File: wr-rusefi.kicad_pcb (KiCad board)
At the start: 2 copper layers, 88.9 x 78.7 mm, 114 parts, among them P101 USB_OTG, P102 CONN_02X20, Q401 IRF540N, Q402 IRF540N, Q403 IRF540N, Q404 IRF540N, Q405 IRF540N, Q406 IRF540N, U101 ISL89410, U102 ISL89410, U103 FT230XS, U104 STM32F373CCTx, U105 MCP2562-E/SN, U106 LD1117S33TR, U107 MAX9924, U201 LM324, U301 LM324, U501 LM2576xx

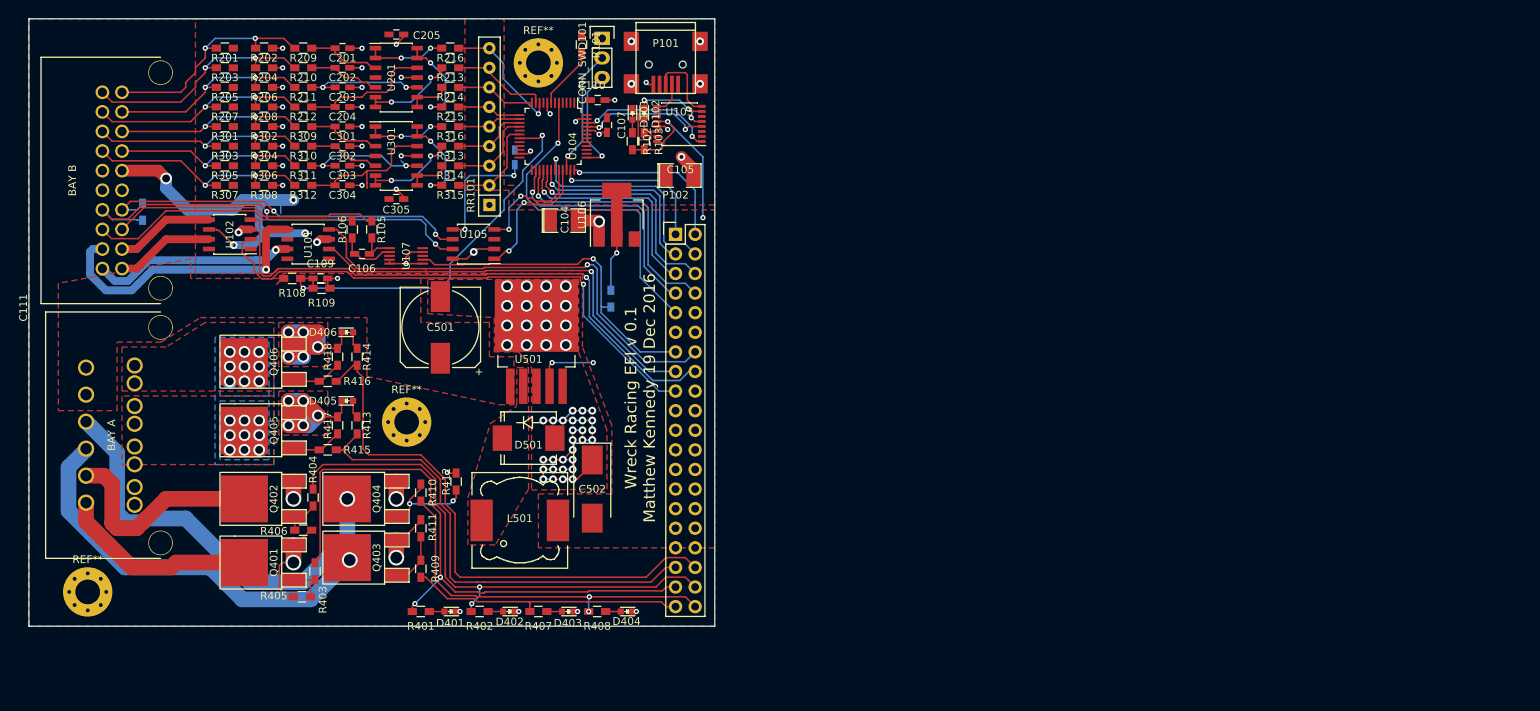
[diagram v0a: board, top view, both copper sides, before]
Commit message: Rework most of board for rusefi
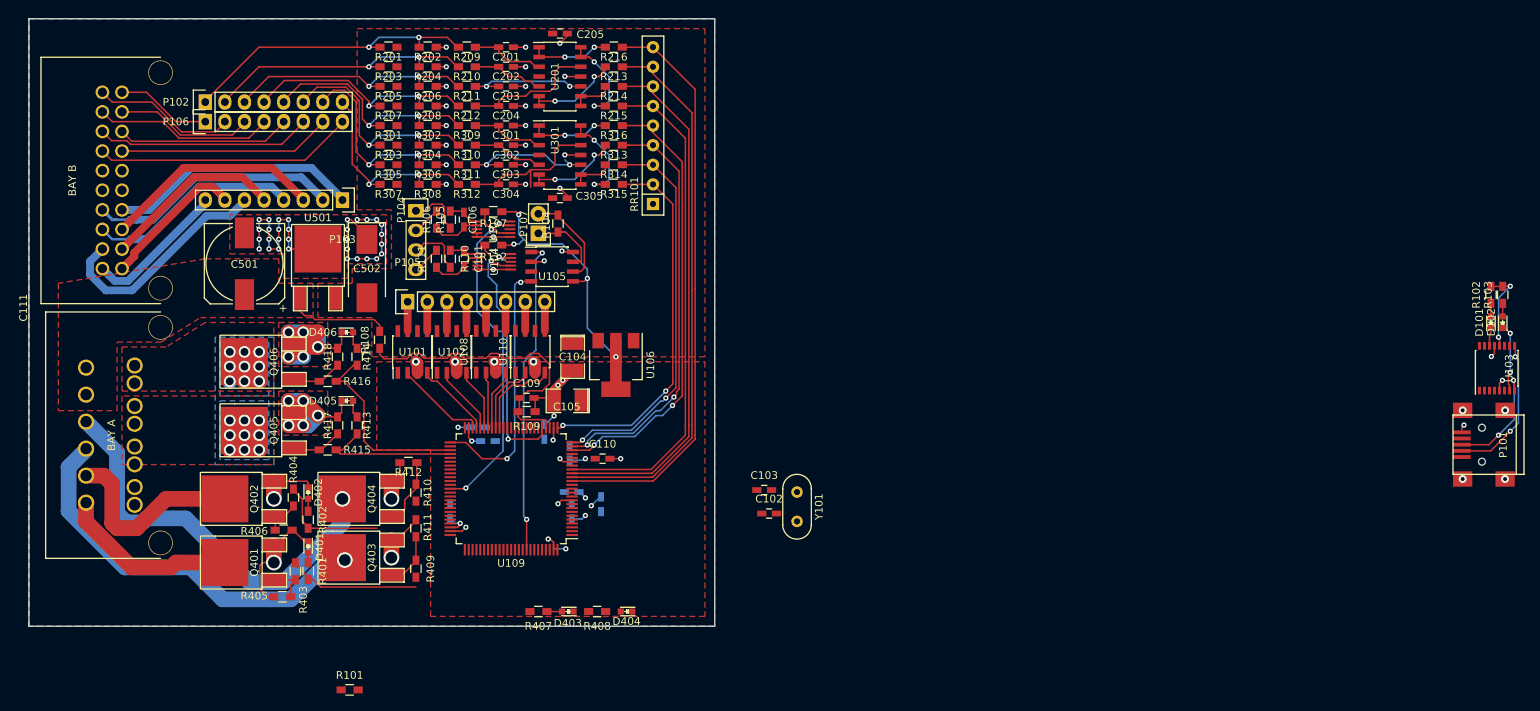
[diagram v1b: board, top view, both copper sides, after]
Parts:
- removed CONN_SWD101: CONN_01X03, Pin_Headers:Pin_Header_Straight_1x03
- removed D501: D_Schottky, Diodes_SMD:SMC_Standard
- removed L501: 38uH, Choke_SMD:Choke_SMD_12x12mm_h6mm
- removed REF** (x3): MountingHole_3.2mm_M3_Pad_Via, Mounting_Holes:MountingHole_3.2mm_M3_Pad_Via
- removed REF***: KiCad-Logo2_12mm_SilkScreen, Symbols:KiCad-Logo2_12mm_SilkScreen
- removed REF***: OSHW-Logo_11.4x12mm_SilkScreen, Symbols:OSHW-Logo_11.4x12mm_SilkScreen
- added C101: 1nF, Capacitors_SMD:C_0603_HandSoldering, F.Cu at (125.0, 83.8)
- added C102: 20pF, Capacitors_SMD:C_0603_HandSoldering, F.Cu at (164.5, 116.8)
- added C103: 20pF, Capacitors_SMD:C_0603_HandSoldering, F.Cu at (163.9, 113.8)
- added C112: 2.2uF, Capacitors_SMD:C_0603_HandSoldering, B.Cu at (128.1, 107.4)
- added C113: 2.2uF, Capacitors_SMD:C_0603_HandSoldering, B.Cu at (123.2, 116.5)
- added C114: .1uF, Capacitors_SMD:C_0603_HandSoldering, B.Cu at (135.4, 106.2)
- added C115: .1uF, Capacitors_SMD:C_0603_HandSoldering, B.Cu at (138.9, 114.0)
- added C116: .1uF, Capacitors_SMD:C_0603_HandSoldering, B.Cu at (138.9, 116.6)
- added C117: 4.7uF, Capacitors_SMD:C_0603_HandSoldering, B.Cu at (142.7, 115.6)
- added P103: CONN_01X08, Socket_Strips:Socket_Strip_Straight_1x08, F.Cu at (109.2, 76.2)
- added P104: CONN_01X04, Socket_Strips:Socket_Strip_Straight_1x04, F.Cu at (118.7, 77.6)
- added P105: CONN_01X08, Socket_Strips:Socket_Strip_Straight_1x08, F.Cu at (117.7, 89.4)
- added P106: CONN_01X08, Socket_Strips:Socket_Strip_Straight_1x08, F.Cu at (91.4, 66.0)
- added P107: CONN_01X02, Socket_Strips:Socket_Strip_Straight_1x02, F.Cu at (134.6, 80.5)
- added R110: 10k, Resistors_SMD:R_0603_HandSoldering, F.Cu at (123.2, 83.8)
- added R111: 10k, Resistors_SMD:R_0603_HandSoldering, F.Cu at (121.4, 83.8)
- added R112: 10k, Resistors_SMD:R_0603_HandSoldering, F.Cu at (128.8, 82.0)
- added U108: ISL89410, Housings_SOIC:SOIC-8_3.9x4.9mm_Pitch1.27mm, F.Cu at (128.5, 95.9)
- added U109: STM32F407VGTx, Housings_QFP:LQFP-100_14x14mm_Pitch0.5mm, F.Cu at (131.1, 113.6)
- added U110: ISL89410, Housings_SOIC:SOIC-8_3.9x4.9mm_Pitch1.27mm, F.Cu at (133.6, 95.9)
- added Y101: Crystal, Crystals:Crystal_HC52-6mm_Vertical, F.Cu at (168.1, 114.1)
- C107: moved to B.Cu
- P102: value CONN_02X20 -> CONN_01X08; footprint Pin_Headers:Pin_Header_Straight_2x20 -> Socket_Strips:Socket_Strip_Straight_1x08
- R104, R107: moved to F.Cu
- U104: value STM32F373CCTx -> MAX9924; footprint Housings_QFP:LQFP-48_7x7mm_Pitch0.5mm -> wr-efi:uMAX-10
- U501: value LM2576xx -> LM7805CT; footprint TO_SOT_Packages_SMD:TO-263-5Lead -> TO_SOT_Packages_SMD:TO-252-2Lead
- moved P101 117.8 mm to (257.8, 107.9), turned to 180 degrees
- moved D101 114.5 mm to (258.1, 92.0), turned to 90 degrees
- moved D102 114.5 mm to (259.6, 92.0), turned to 90 degrees
- moved R102 113.1 mm to (258.1, 88.5), turned to 90 degrees
- moved R103 113.1 mm to (259.6, 88.5), turned to 90 degrees
- moved U103 110.6 mm to (258.9, 98.0), turned to 90 degrees
- moved R101 88.9 mm to (110.2, 139.7), turned to 0 degrees
- moved P102 63.3 mm to (91.4, 63.5)
- moved R104 53.9 mm to (137.2, 79.2)
- moved C110 46.5 mm to (142.9, 109.7)
- moved C107 42.6 mm to (126.8, 105.7), turned to 0 degrees
- moved C502 40.9 mm to (112.4, 85.1)
- moved C108 38.9 mm to (138.7, 109.0)
- moved C105 32.6 mm to (138.4, 102.2), turned to 180 degrees
- moved U102 32.6 mm to (123.4, 95.9), turned to 90 degrees
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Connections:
- C111 pad 11: IGN_A_OUT -> Net-(C111-Pad11)
- C111 pad 12: IGN_B_OUT -> Net-(C111-Pad12)
- C111 pad 13: VR- -> Net-(C111-Pad13)
- C111 pad 14: CANH -> Net-(C111-Pad14)
- C111 pad 17: AIN7 -> Net-(C111-Pad17)
- C111 pad 18: AIN5 -> Net-(C111-Pad18)
- C111 pad 19: AIN3 -> Net-(C111-Pad19)
- C111 pad 20: AIN1 -> Net-(C111-Pad20)
- C111 pad 21: IGN_C_OUT -> Net-(C111-Pad21)
- C111 pad 22: IGN_D_OUT -> Net-(C111-Pad22)
- C111 pad 23: VR+ -> Net-(C111-Pad23)
- C111 pad 24: CANL -> Net-(C111-Pad24)
- C111 pad 27: AIN6 -> Net-(C111-Pad27)
- C111 pad 28: AIN4 -> Net-(C111-Pad28)
- C111 pad 29: AIN2 -> Net-(C111-Pad29)
- C111 pad 30: AIN0 -> Net-(C111-Pad30)
- P102 pad 1: FPGA_G2 -> AIN0
- P102 pad 2: FPGA_G1 -> AIN1
- P102 pad 3: FPGA_G4 -> AIN2
- P102 pad 4: FPGA_G3 -> AIN3
- P102 pad 5: FPGA_SCK -> AIN4
- P102 pad 6: FPGA_G5 -> AIN5
- P102 pad 7: FPGA_MISO -> AIN6
- P102 pad 8: FPGA_MOSI -> AIN7
- R105 pad 2: VR+ -> VR1+
- R106 pad 2: VR- -> VR1-
- R107 pad 1: VRIN -> VRIN1
- U104 pad 1: +3V3 -> Net-(C101-Pad1)
- U104 pad 10: a0 -> +5V
- U104 pad 4: Net-(U104-Pad4) -> GND
- U104 pad 5: FPGA_MCU_CLK -> GND
- U104 pad 6: Net-(U104-Pad6) -> GND
- U104 pad 7: Net-(R101-Pad2) -> VRIN2
- U104 pad 8: GND -> Net-(U104-Pad8)
- U104 pad 9: +3V3 -> GND
- U107 pad 7: VRIN -> VRIN1
- U501 pad 2: Net-(D501-Pad1) -> GND
- U501 pad 3: GND -> +5V
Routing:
- net +5V: track 82.7 -> 10.9 mm, vias 8 -> 2
- net IGN_D_IN: track 74.3 -> 8.08 mm, vias 1 -> 0
- net IGN_C_IN: track 70.2 -> 8.93 mm, vias 1 -> 0
- net ls_1: track 77.9 -> 17.5 mm, vias 2 -> 0
- net a1: track 12.8 -> 71.8 mm
- net a0: track 16.6 -> 75.4 mm, vias 1 -> 0
- net a2: track 10.3 -> 68.4 mm
- net a3: track 8.32 -> 64.9 mm
- net ls_2: track 69.9 -> 14.8 mm, vias 2 -> 0
- net IGN_B_IN: track 60.3 -> 10.2 mm, vias 1 -> 0
- net a4: track 8.29 -> 57.8 mm, vias 0 -> 2
- net ls_4: track 48.0 -> 0.00 mm, vias 2 -> 0
- net INJ_B_IN: track 72.7 -> 25.2 mm
- net CANH: track 56.1 -> 9.31 mm, vias 2 -> 0
- net VRIN1: track 0.00 -> 45.5 mm, vias 0 -> 2
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- removed copper zone on F.Cu, net Net-(D501-Pad1)
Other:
- board text removed: "Wreck Racing EFI v 0.1 Matthew Kennedy 19 Dec 2016"

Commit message: Board mostly complete
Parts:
- added P108: USB_OTG, Connect:USB_Mini-B, F.Cu at (152.1, 124.3)
- added P109: CONN_01X02, Socket_Strips:Socket_Strip_Straight_1x02, F.Cu at (126.0, 126.7)
- added P110: CONN_01X06, Socket_Strips:Socket_Strip_Straight_1x06, F.Cu at (119.6, 129.3)
- added R113: 10k, Resistors_SMD:R_0603_HandSoldering, F.Cu at (128.5, 125.6)
- C102, C103, R101: moved to B.Cu
- Y101: footprint Crystals:Crystal_HC52-6mm_Vertical -> Crystals:Crystal_HC49-U_Vertical
- moved D102 130.8 mm to (132.9, 124.2), turned to 0 degrees
- moved D101 129.7 mm to (132.9, 125.7), turned to 0 degrees
- moved R103 128.4 mm to (136.3, 124.2), turned to 0 degrees
- moved R102 127.4 mm to (136.3, 125.7), turned to 0 degrees
- moved U103 119.7 mm to (142.2, 125.0), turned to 180 degrees
- moved P101 105.2 mm to (152.7, 112.9)
- moved R101 43.4 mm to (142.2, 110.5), turned to 270 degrees
- moved D404 40.7 mm to (110.2, 110.2), turned to 0 degrees
- moved R408 34.6 mm to (113.5, 110.2), turned to 0 degrees
- moved Y101 24.6 mm to (143.5, 113.8)
- moved C102 22.9 mm to (141.7, 118.9), turned to 90 degrees
- moved C103 22.2 mm to (141.7, 114.8), turned to 270 degrees
- moved D403 20.6 mm to (119.9, 120.7), turned to 270 degrees
- moved R407 15.8 mm to (119.9, 124.0), turned to 270 degrees
- moved C117 9.11 mm to (135.7, 121.4), turned to 180 degrees
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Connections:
- R101 pad 2: Net-(R101-Pad2) -> NRST
- U109 pad 14: Net-(U109-Pad14) -> NRST
- U109 pad 55: ls_1 -> ls_4
- U109 pad 58: ls_4 -> ls_1
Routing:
- net +5V: track 10.9 -> 88.9 mm, vias 2 -> 3
- net Net-(P108-Pad1): track 0.00 -> 44.0 mm
- net NRST: track 0.00 -> 43.6 mm, vias 0 -> 2
- net Net-(P108-Pad2): track 0.00 -> 42.7 mm
- net Net-(P108-Pad3): track 0.00 -> 41.5 mm
- net ftdi_rx: track 0.00 -> 25.2 mm, vias 0 -> 2
- net ftdi_tx: track 0.00 -> 23.4 mm, vias 0 -> 2
- net Net-(P110-Pad4): track 0.00 -> 20.0 mm, vias 0 -> 2
- net ls_3: track 0.00 -> 18.9 mm
- net ls_1: track 17.5 -> 36.2 mm
- net ls_2: track 14.8 -> 31.3 mm
- net ls_4: track 0.00 -> 15.3 mm
- net Net-(P110-Pad2): track 0.00 -> 13.2 mm, vias 0 -> 2
- net Net-(P109-Pad1): track 0.00 -> 11.8 mm, vias 0 -> 2
- net GND: track 191.5 -> 201.3 mm, vias 90 -> 97
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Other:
- rule trace_min: 0.1524 -> 0.2032

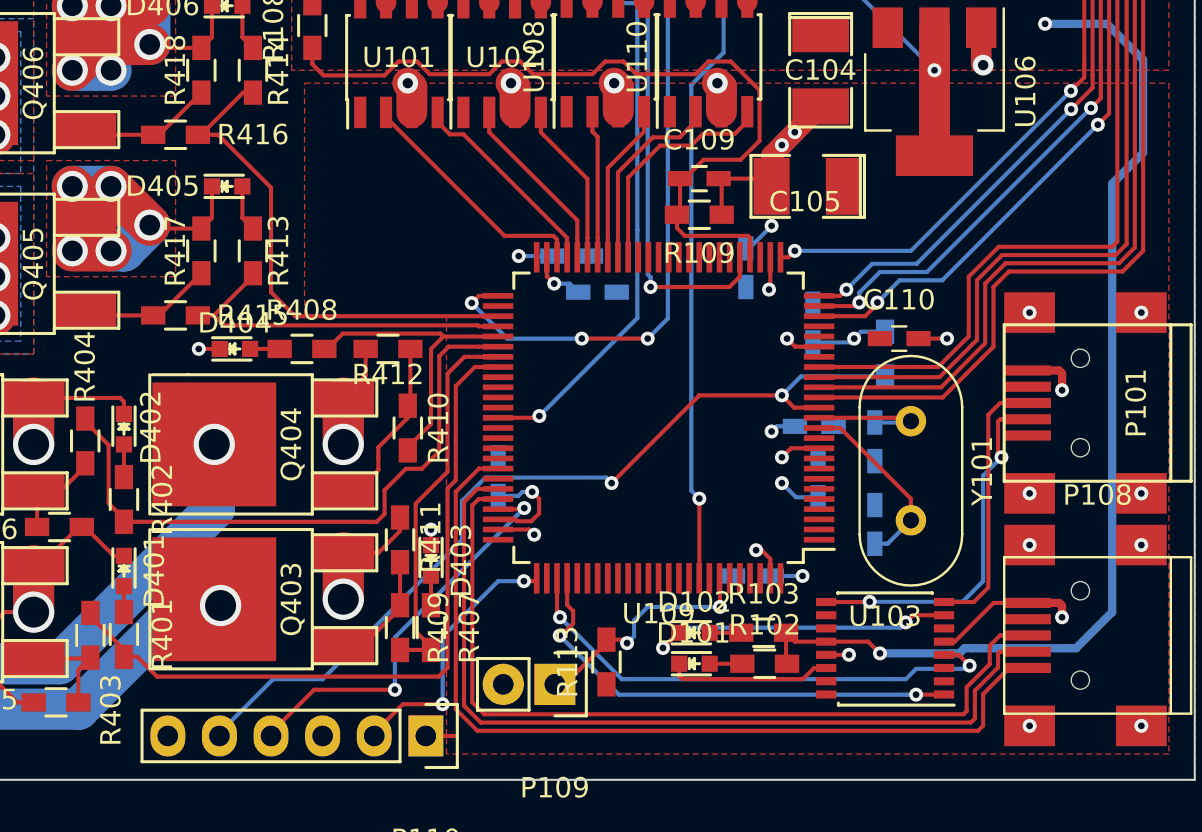
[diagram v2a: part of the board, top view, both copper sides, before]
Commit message: Add debug LEDs, power via 2nd USB
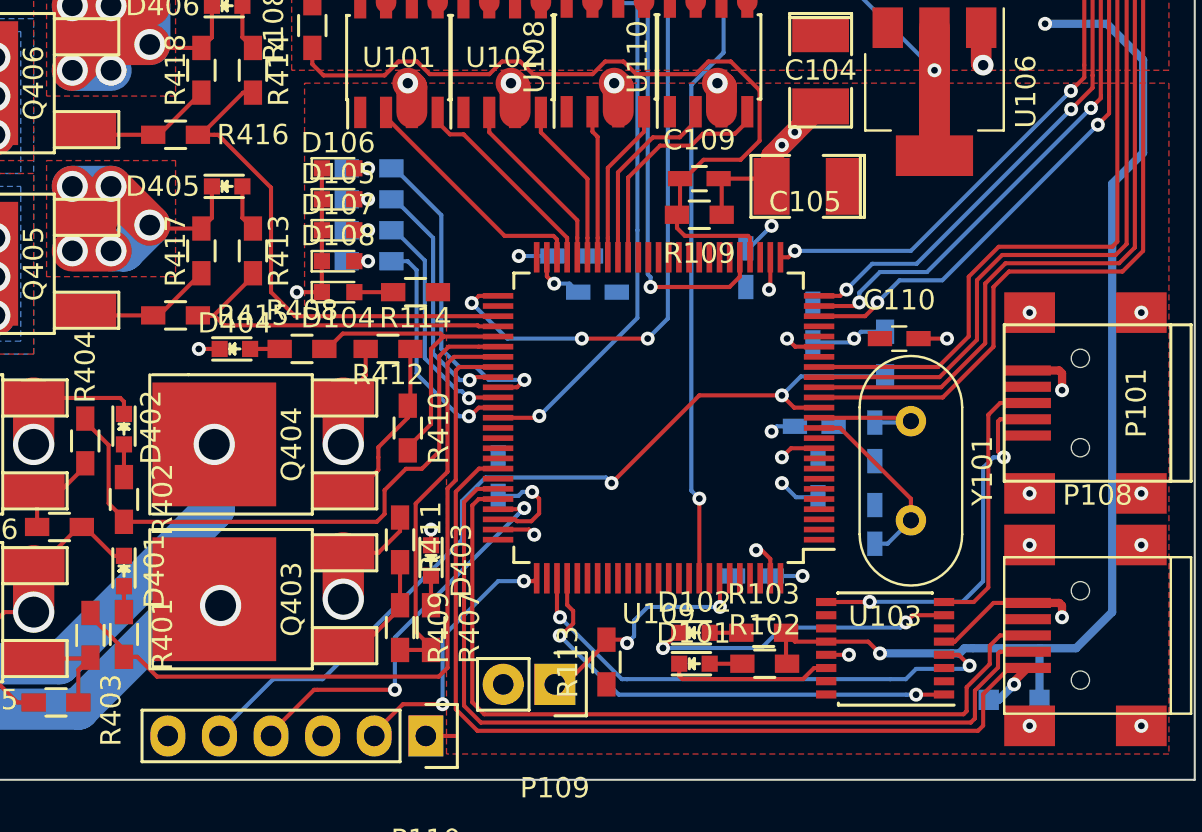
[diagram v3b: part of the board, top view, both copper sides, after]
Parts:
- added D103: PMEG2010EA, Diodes_SMD:D_SOD-323_HandSoldering, B.Cu at (148.6, 127.5)
- added D104: LED, LEDs:LED_0603, F.Cu at (115.3, 107.4)
- added D105: LED, LEDs:LED_0603, F.Cu at (115.3, 102.9)
- added D106: LED, LEDs:LED_0603, F.Cu at (115.3, 101.3)
- added D107: LED, LEDs:LED_0603, F.Cu at (115.3, 104.4)
- added D108: LED, LEDs:LED_0603, F.Cu at (115.3, 105.9)
- added R114: 1k, Resistors_SMD:R_0603_HandSoldering, F.Cu at (119.1, 107.4)
- added R115: 1k, Resistors_SMD:R_0603_HandSoldering, B.Cu at (116.8, 102.9)
- added R116: 1k, Resistors_SMD:R_0603_HandSoldering, B.Cu at (116.8, 101.3)
- added R117: 1k, Resistors_SMD:R_0603_HandSoldering, B.Cu at (116.8, 104.4)
- added R118: 1k, Resistors_SMD:R_0603_HandSoldering, B.Cu at (116.8, 105.9)
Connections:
- U109 pad 59: Net-(U109-Pad59) -> PD12
- U109 pad 60: Net-(U109-Pad60) -> PD13
- U109 pad 61: Net-(U109-Pad61) -> PD14
- U109 pad 62: Net-(U109-Pad62) -> PD15
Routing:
- net PD13: track 0.00 -> 16.2 mm, vias 0 -> 1
- net PD12: track 0.00 -> 12.3 mm, vias 0 -> 1
- net PD15: track 0.00 -> 11.6 mm, vias 0 -> 1
- net PD14: track 0.00 -> 11.5 mm, vias 0 -> 1
- net GND: track 201.3 -> 208.6 mm, vias 97 -> 98
- net Net-(D103-Pad2): track 44.0 -> 46.7 mm, vias 0 -> 1
- net +5V: track 88.9 -> 91.5 mm
- net Net-(D104-Pad2): track 0.00 -> 1.91 mm
- net Net-(D108-Pad2): track 0.00 -> 1.73 mm, vias 0 -> 1
- net Net-(D107-Pad2): track 0.00 -> 1.73 mm, vias 0 -> 1
- net Net-(D106-Pad2): track 0.00 -> 1.73 mm, vias 0 -> 1
- net Net-(D105-Pad2): track 0.00 -> 1.73 mm, vias 0 -> 1
- net ls_out_4: track 54.5 -> 53.2 mm
